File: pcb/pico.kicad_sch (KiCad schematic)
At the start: 13 parts, among them J5 Conn_01x20_Pin, J6 Conn_01x20_Pin, M1 FL, M2 FR, M3 RL, M4 RR, U1 TB9051FTG, U14 IR_Transmitter, U2 TB9051FTG, U3 TB9051FTG, U4 TB9051FTG, U6 SN74LVC8T245NSR

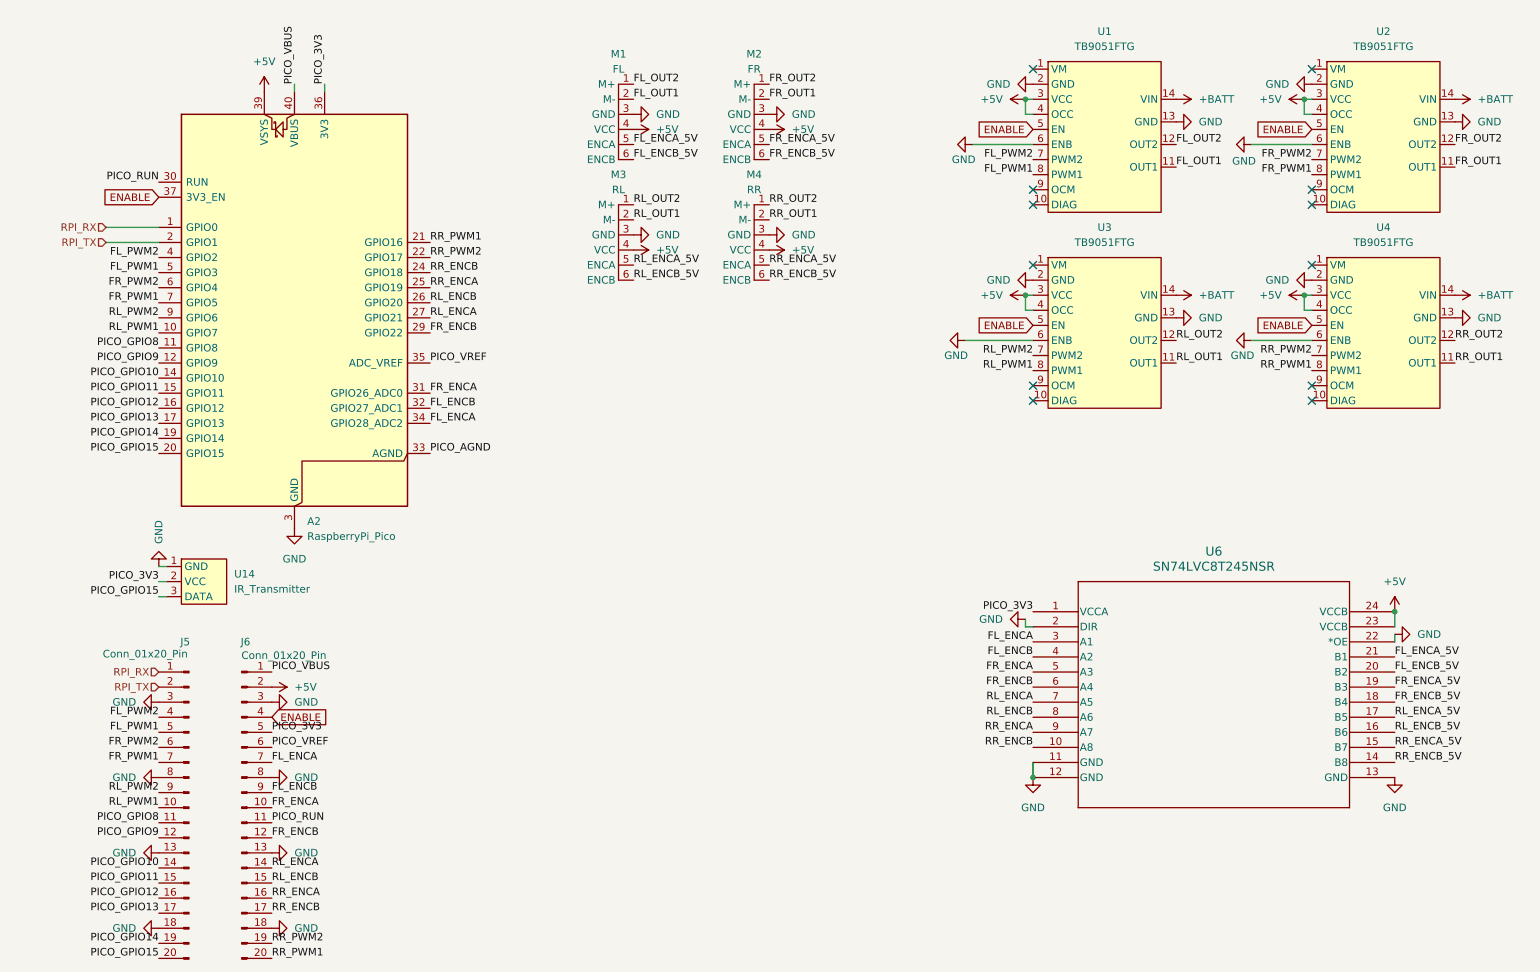
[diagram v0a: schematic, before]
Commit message: Fix ERC issues and layout connectors
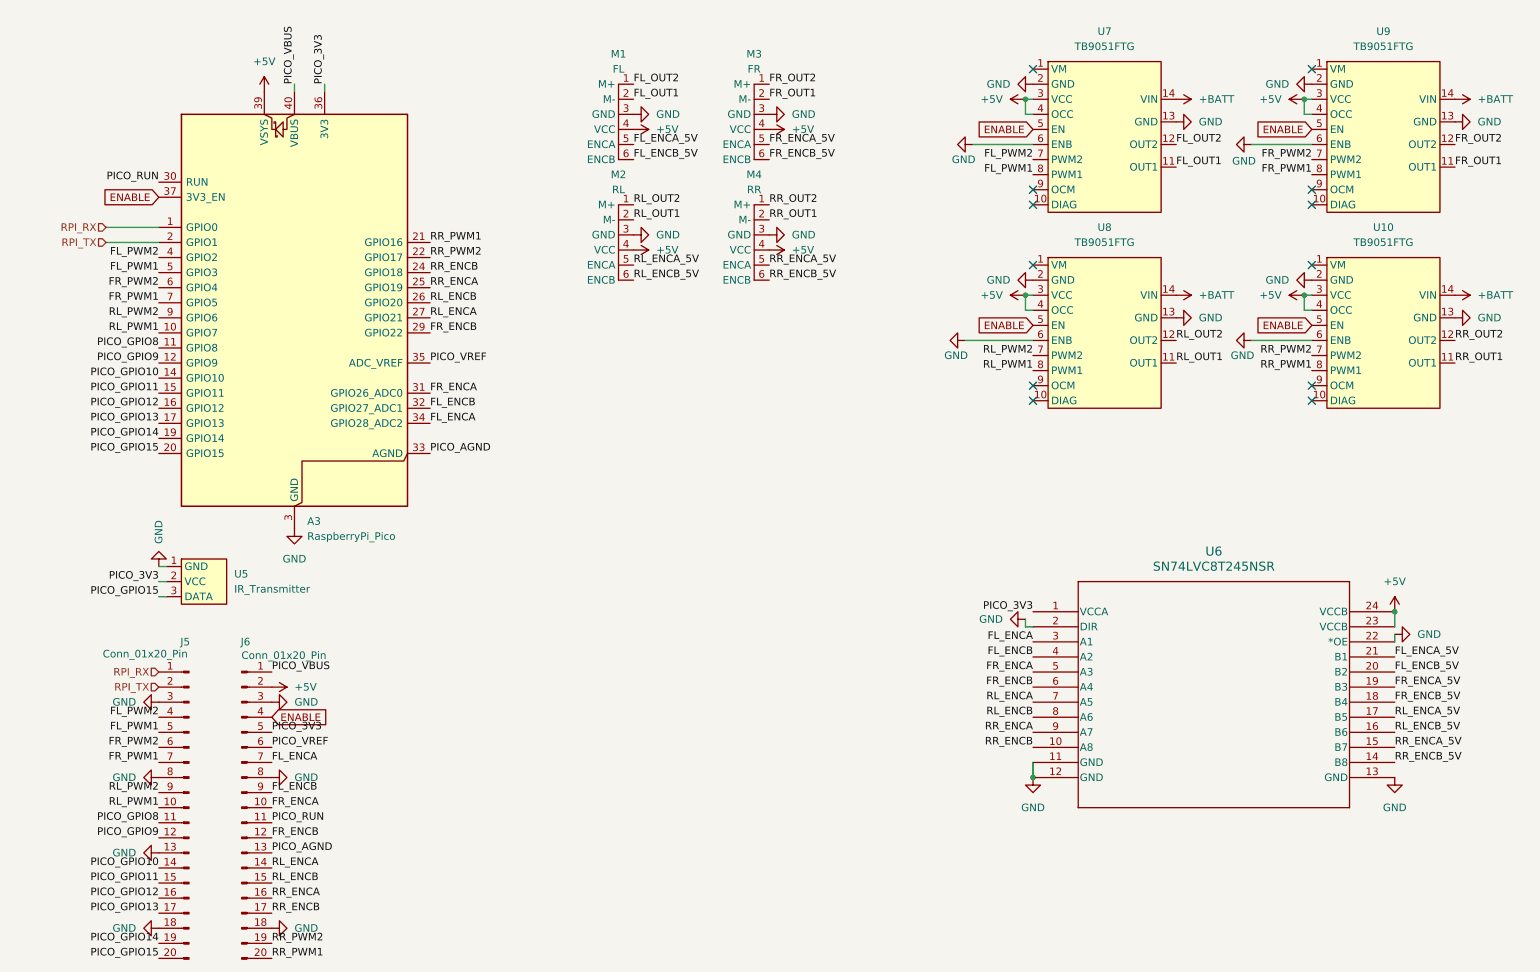
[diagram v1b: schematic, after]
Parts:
- renumbered A2 to A3, M3 to M2, M2 to M3, U4 to U10, U14 to U5, U1 to U7, U3 to U8, U2 to U9
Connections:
- net GND: no longer J6.13 (Pin_13)
- net PICO_AGND: now also J6.13 (Pin_13)

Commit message: Start routing
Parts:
- renumbered A3 to A?, J6 to J?, J5 to J?, M4 to M?, M1 to M?, M2 to M?, M3 to M?, U7 to U?, U9 to U?, U8 to U?, U10 to U?, U6 to U?, U5 to U?
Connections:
- net GND: now also J?.13 (Pin_13); no longer J?.8 (Pin_8)
- net PICO_AGND: now also J?.8 (Pin_8); no longer J?.13 (Pin_13)

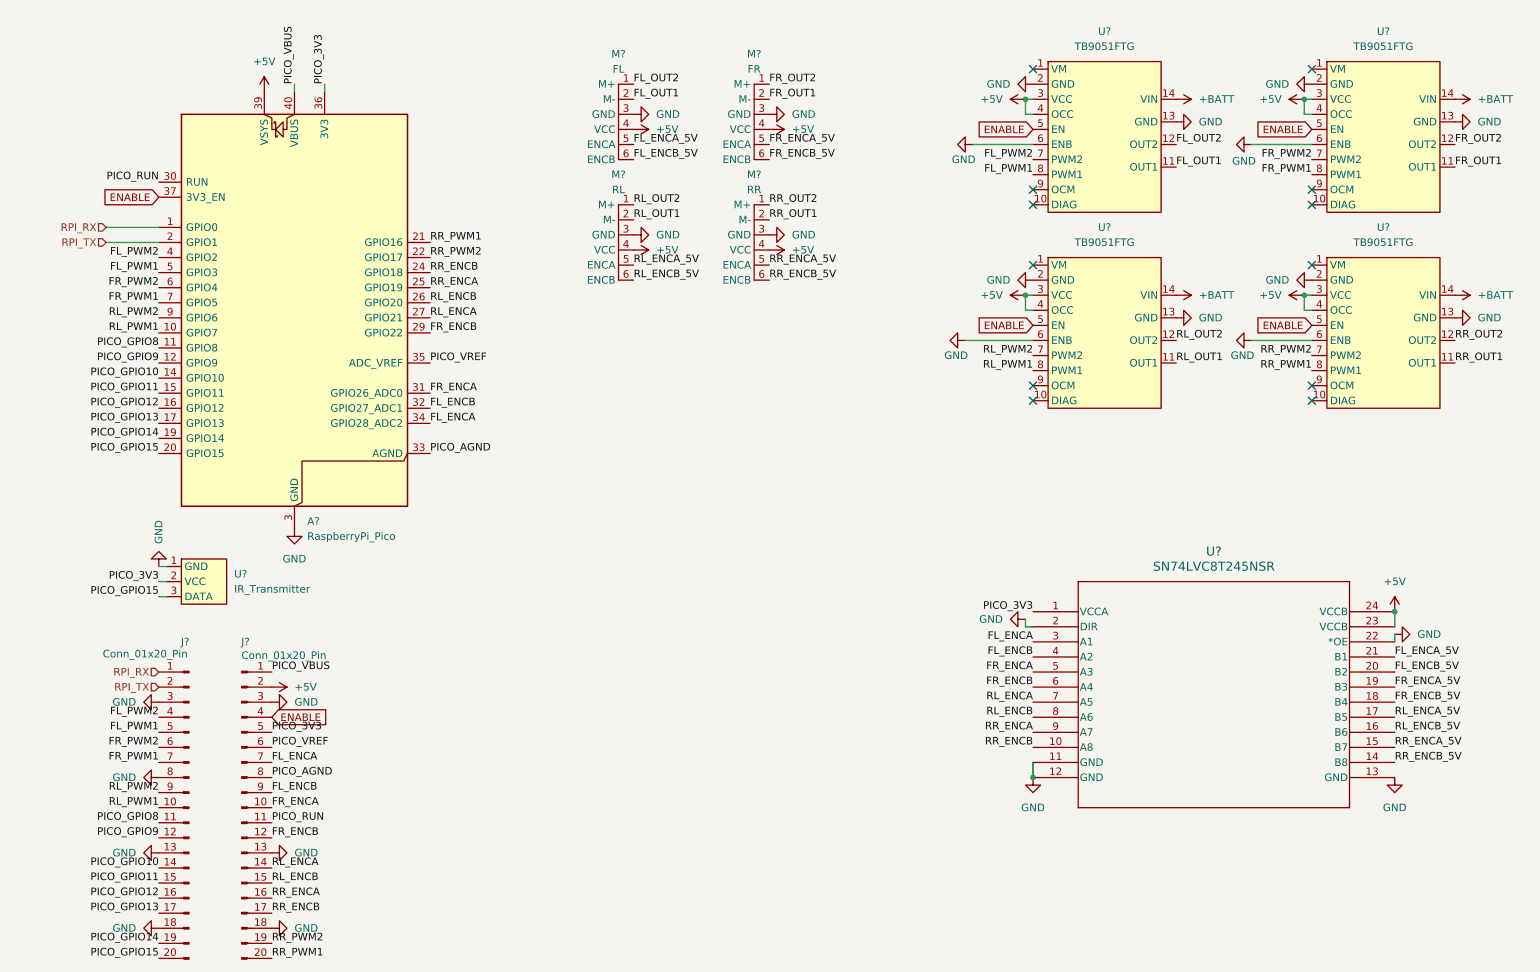
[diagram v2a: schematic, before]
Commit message: Route I2C and planes
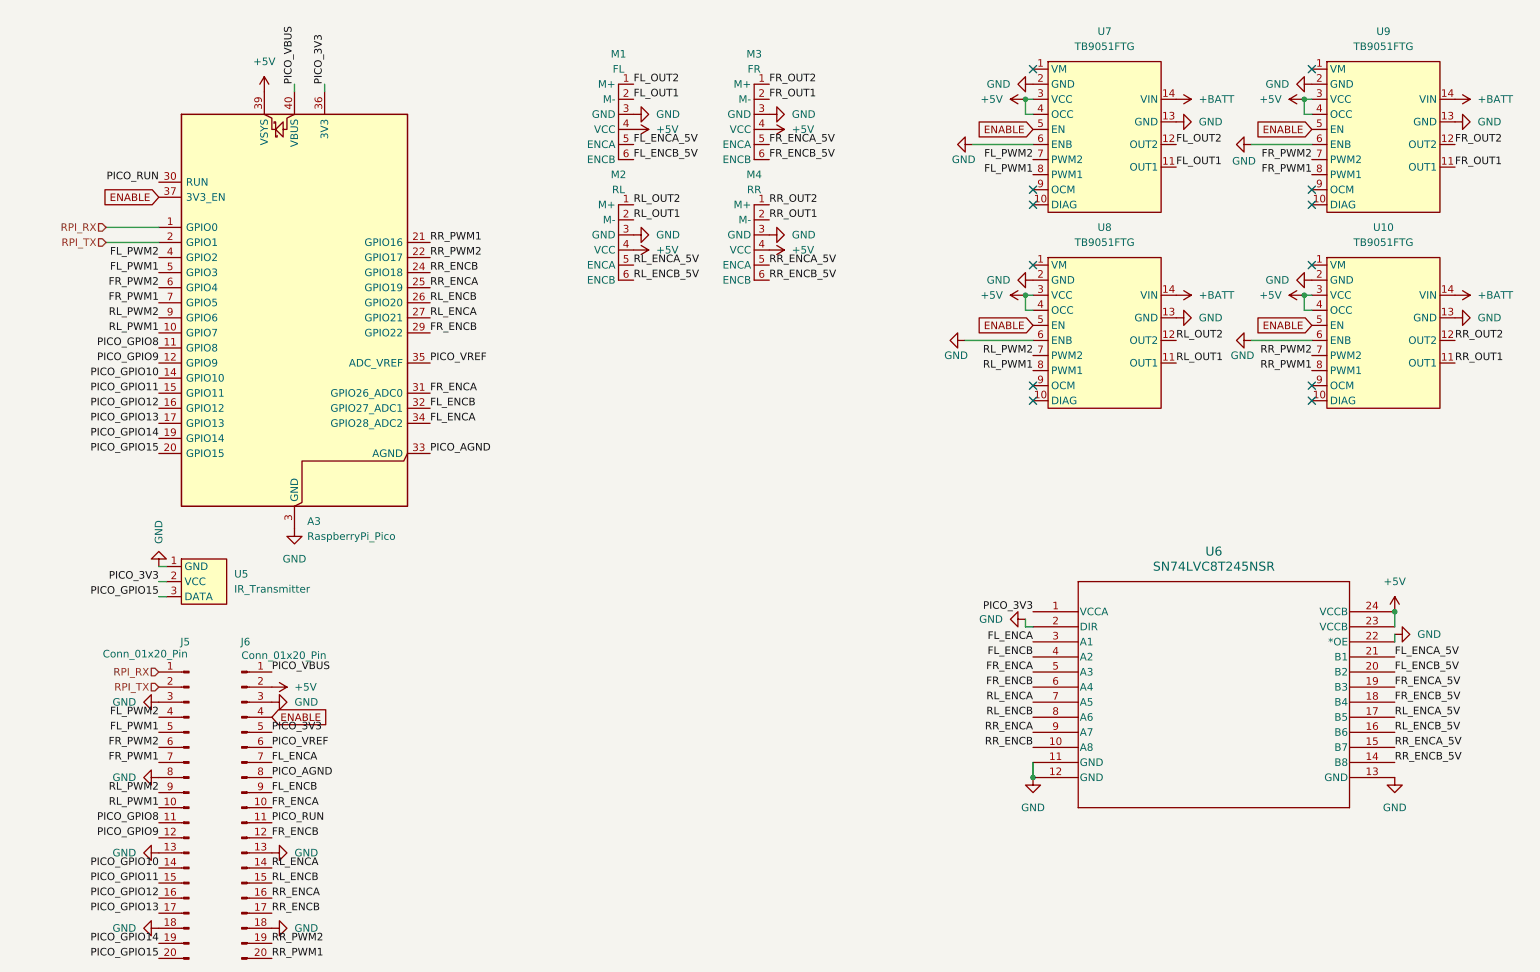
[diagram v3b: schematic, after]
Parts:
- gave numbers to parts that had none: 13
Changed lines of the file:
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@@
 		(dnp no)
 		(fields_autoplaced yes)
-		(property "Reference" "#PWR?"
+		(property "Reference" "#PWR039"
 			(at 129.54 35.56 0)
 			(effects
@@
 		(dnp no)
 		(fields_autoplaced yes)
-		(property "Reference" "#PWR?"
+		(property "Reference" "#PWR030"
 			(at 46.99 157.48 0)
 			(effects
@@
 		(dnp no)
 		(fields_autoplaced yes)
-		(property "Reference" "#PWR?"
+		(property "Reference" "#PWR066"
 			(at 261.62 151.13 0)
 			(effects
@@
 		(dnp no)
 		(fields_autoplaced yes)
-		(property "Reference" "#PWR01"
+		(property "Reference" "#PWR0101"
 			(at 78.74 157.48 0)
 			(effects
@@
 				)
 			)
+			(project "ieee"
+				(path "/de247b43-2c3b-4650-9f65-a404f4d1ae86/a87090f9-d2e3-4dff-b75c-ef59f3dcab82"
+					(reference "#PWR0101")
+					(unit 1)
+				)
+			)
 		)
 	)
@@
 		(dnp no)
 		(fields_autoplaced yes)
-		(property "Reference" "#PWR?"
+		(property "Reference" "#PWR056"
 			(at 220.98 63.5 0)
 			(effects
@@
 		(dnp no)
 		(fields_autoplaced yes)
-		(property "Reference" "#PWR?"
+		(property "Reference" "#PWR048"
 			(at 203.2 30.48 0)
 			(effects
@@
 		(dnp no)
 		(fields_autoplaced yes)
-		(property "Reference" "#PWR?"
+		(property "Reference" "#PWR068"
 			(at 278.13 34.29 0)
 			(effects
@@
 		(dnp no)
 		(fields_autoplaced yes)
-		(property "Reference" "#PWR?"
+		(property "Reference" "#PWR061"
 			(at 250.19 63.5 0)
 			(effects
@@
 		(dnp no)
 		(fields_autoplaced yes)
-		(property "Reference" "#PWR?"
+		(property "Reference" "#PWR052"
 			(at 194.31 60.96 0)
 			(effects
@@
 		(dnp no)
 		(fields_autoplaced yes)
-		(property "Reference" "#PWR?"
+		(property "Reference" "#PWR033"
 			(at 68.58 129.54 0)
 			(effects
@@
 		(dnp no)
 		(fields_autoplaced yes)
-		(property "Reference" "#PWR?"
+		(property "Reference" "#PWR031"
 			(at 46.99 170.18 0)
 			(effects
@@
 		(dnp no)
 		(fields_autoplaced yes)
-		(property "Reference" "#PWR?"
+		(property "Reference" "#PWR040"
 			(at 139.7 53.34 0)
 			(effects
@@
 		(dnp no)
 		(fields_autoplaced yes)
-		(property "Reference" "#PWR?"
+		(property "Reference" "#PWR051"
 			(at 194.31 27.94 0)
 			(effects
@@
 		(on_board yes)
 		(dnp no)
-		(property "Reference" "#PWR?"
+		(property "Reference" "#PWR058"
 			(at 231.14 38.1 0)
 			(effects
@@
 		(dnp no)
 		(fields_autoplaced yes)
-		(property "Reference" "#PWR?"
+		(property "Reference" "#PWR042"
 			(at 162.56 33.02 0)
 			(effects
@@
 		(on_board yes)
 		(dnp no)
-		(property "Reference" "#PWR?"
+		(property "Reference" "#PWR050"
 			(at 193.04 118.11 0)
 			(effects
@@
 		(dnp no)
 		(fields_autoplaced yes)
-		(property "Reference" "#PWR?"
+		(property "Reference" "#PWR055"
 			(at 231.14 34.29 0)
 			(effects
@@
 		(dnp no)
 		(fields_autoplaced yes)
-		(property "Reference" "U?"
+		(property "Reference" "U7"
 			(at 212.725 19.05 0)
 			(effects
@@
 		(dnp no)
 		(fields_autoplaced yes)
-		(property "Reference" "#PWR?"
+		(property "Reference" "#PWR044"
 			(at 162.56 53.34 0)
 			(effects
@@
 		(on_board yes)
 		(dnp no)
-		(property "Reference" "#PWR?"
+		(property "Reference" "#PWR032"
 			(at 71.12 33.02 0)
 			(effects
@@
 		(on_board yes)
 		(dnp no)
-		(property "Reference" "J?"
+		(property "Reference" "J6"
 			(at 67.945 121.92 0)
 			(effects
@@
 		(dnp no)
 		(fields_autoplaced yes)
-		(property "Reference" "U?"
+		(property "Reference" "U9"
 			(at 259.715 19.05 0)
 			(effects
@@
 		(dnp no)
 		(fields_autoplaced yes)
-		(property "Reference" "#PWR?"
+		(property "Reference" "#PWR064"
 			(at 261.62 120.65 0)
 			(effects
@@
 		(dnp no)
 		(fields_autoplaced yes)
-		(property "Reference" "#PWR?"
+		(property "Reference" "#PWR070"
 			(at 278.13 67.31 0)
 			(effects
@@
 		(on_board yes)
 		(dnp no)
-		(property "Reference" "#PWR?"
+		(property "Reference" "#PWR027"
 			(at 53.34 102.87 0)
 			(effects
@@
 		(dnp no)
 		(fields_autoplaced yes)
-		(property "Reference" "#PWR?"
+		(property "Reference" "#PWR028"
 			(at 46.99 132.08 0)
 			(effects
@@
 		(dnp no)
 		(fields_autoplaced yes)
-		(property "Reference" "#PWR?"
+		(property "Reference" "#PWR029"
 			(at 46.99 144.78 0)
 			(effects
@@
 		(dnp no)
 		(fields_autoplaced yes)
-		(property "Reference" "#PWR?"
+		(property "Reference" "#PWR067"
 			(at 267.97 30.48 0)
 			(effects
@@
 		(on_board yes)
 		(dnp no)
-		(property "Reference" "#PWR?"
+		(property "Reference" "#PWR047"
 			(at 184.15 38.1 0)
 			(effects
@@
 		(dnp no)
 		(fields_autoplaced yes)
-		(property "Reference" "U?"
+		(property "Reference" "U8"
 			(at 212.725 52.07 0)
 			(effects
@@
 		(dnp no)
 		(fields_autoplaced yes)
-		(property "Reference" "#PWR?"
+		(property "Reference" "#PWR060"
 			(at 250.19 30.48 0)
 			(effects
@@
 		(on_board yes)
 		(dnp no)
-		(property "Reference" "U?"
+		(property "Reference" "U10"
 			(at 259.715 52.07 0)
 			(effects
@@
 		(dnp no)
 		(fields_autoplaced yes)
-		(property "Reference" "M?"
+		(property "Reference" "M4"
 			(at 153.67 43.18 0)
 			(effects
@@
 		(dnp no)
 		(fields_autoplaced yes)
-		(property "Reference" "#PWR?"
+		(property "Reference" "#PWR049"
 			(at 203.2 63.5 0)
 			(effects
@@
 		(dnp no)
 		(fields_autoplaced yes)
-		(property "Reference" "M?"
+		(property "Reference" "M1"
 			(at 130.81 22.86 0)
 			(effects
@@
 		(dnp no)
 		(fields_autoplaced yes)
-		(property "Reference" "U?"
+		(property "Reference" "U6"
 			(at 231.14 106.68 0)
 			(effects
@@
 		(on_board yes)
 		(dnp no)
-		(property "Reference" "#PWR?"
+		(property "Reference" "#PWR059"
 			(at 231.14 71.12 0)
 			(effects
@@
 		(dnp no)
 		(fields_autoplaced yes)
-		(property "Reference" "#PWR?"
+		(property "Reference" "#PWR036"
 			(at 78.74 170.18 0)
 			(effects
@@
 		(dnp no)
 		(fields_autoplaced yes)
-		(property "Reference" "M?"
+		(property "Reference" "M2"
 			(at 130.81 43.18 0)
 			(effects
@@
 		(dnp no)
 		(fields_autoplaced yes)
-		(property "Reference" "#PWR?"
+		(property "Reference" "#PWR053"
 			(at 200.66 151.13 0)
 			(effects
@@
 		(dnp no)
 		(fields_autoplaced yes)
-		(property "Reference" "#PWR?"
+		(property "Reference" "#PWR045"
 			(at 152.4 55.88 0)
 			(effects
@@
 		(dnp no)
 		(fields_autoplaced yes)
-		(property "Reference" "#PWR?"
+		(property "Reference" "#PWR062"
 			(at 241.3 27.94 0)
 			(effects
@@
 		(dnp no)
 		(fields_autoplaced yes)
-		(property "Reference" "#PWR?"
+		(property "Reference" "#PWR057"
 			(at 231.14 67.31 0)
 			(effects
@@
 		(dnp no)
 		(fields_autoplaced yes)
-		(property "Reference" "#PWR?"
+		(property "Reference" "#PWR054"
 			(at 220.98 30.48 0)
 			(effects
@@
 		(dnp no)
 		(fields_autoplaced yes)
-		(property "Reference" "#PWR?"
+		(property "Reference" "#PWR038"
 			(at 139.7 33.02 0)
 			(effects
@@
 		(dnp no)
 		(fields_autoplaced yes)
-		(property "Reference" "#PWR?"
+		(property "Reference" "#PWR065"
 			(at 267.97 120.65 0)
 			(effects
@@
 		(dnp no)
 		(fields_autoplaced yes)
-		(property "Reference" "#PWR?"
+		(property "Reference" "#PWR041"
 			(at 129.54 55.88 0)
 			(effects
@@
 		(dnp no)
 		(fields_autoplaced yes)
-		(property "Reference" "#PWR?"
+		(property "Reference" "#PWR043"
 			(at 152.4 35.56 0)
 			(effects
@@
 		(dnp no)
 		(fields_autoplaced yes)
-		(property "Reference" "#PWR?"
+		(property "Reference" "#PWR034"
 			(at 78.74 132.08 0)
 			(effects
@@
 		(on_board yes)
 		(dnp no)
-		(property "Reference" "J?"
+		(property "Reference" "J5"
 			(at 57.785 121.92 0)
 			(effects
@@
 		(on_board yes)
 		(dnp no)
-		(property "Reference" "#PWR?"
+		(property "Reference" "#PWR046"
 			(at 182.88 71.12 0)
 			(effects
@@
 		(dnp no)
 		(fields_autoplaced yes)
-		(property "Reference" "U?"
+		(property "Reference" "U5"
 			(at 66.04 110.4899 0)
 			(effects
@@
 		(dnp no)
 		(fields_autoplaced yes)
-		(property "Reference" "M?"
+		(property "Reference" "M3"
 			(at 153.67 22.86 0)
 			(effects
@@
 		(on_board yes)
 		(dnp no)
-		(property "Reference" "A?"
+		(property "Reference" "A3"
 			(at 78.3433 101.6 0)
 			(effects
@@
 		(dnp no)
 		(fields_autoplaced yes)
-		(property "Reference" "#PWR?"
+		(property "Reference" "#PWR069"
 			(at 267.97 63.5 0)
 			(effects
@@
 		(dnp no)
 		(fields_autoplaced yes)
-		(property "Reference" "#PWR?"
+		(property "Reference" "#PWR037"
 			(at 76.2 109.22 0)
 			(effects
@@
 		(dnp no)
 		(fields_autoplaced yes)
-		(property "Reference" "#PWR?"
+		(property "Reference" "#PWR063"
 			(at 241.3 60.96 0)
 			(effects

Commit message: Finish layout
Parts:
- added C1, C2, C3, C4, C5: 0.1uF, Capacitor_SMD:C_0603_1608Metric_Pad1.08x0.95mm_HandSolder, symbol Device:C
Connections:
- net PICO_GPIO8 is gone; now on net FL_PWM1: A3.11 (GPIO8), J5.11 (Pin_11)
- net PICO_GPIO9 is gone; now on net FL_PWM2: A3.12 (GPIO9), J5.12 (Pin_12)
- net +5V: now also C1.2, C2.2, C4.2
- net FL_PWM1: no longer A3.5 (GPIO3), J5.5 (Pin_5)
- net FL_PWM2: no longer A3.4 (GPIO2), J5.4 (Pin_4)
- net FR_ENCA_5V: now also U6.17 (B5); no longer U6.19 (B3)
- net FR_ENCB_5V: now also U6.16 (B6); no longer U6.18 (B4)
- net FR_PWM1: now also A3.6 (GPIO4), J5.6 (Pin_6); no longer A3.7 (GPIO5), J5.7 (Pin_7)
- net FR_PWM2: now also A3.7 (GPIO5), J5.7 (Pin_7); no longer A3.6 (GPIO4), J5.6 (Pin_6)
- net GND: now also C1.1, C2.1, C3.1, C4.1, C5.1
- net PICO_3V3: now also C3.2, C5.2
- net PICO_GPIO10: now also U5.3 (DATA)
- net PICO_GPIO15: no longer U5.3 (DATA)
- net RL_ENCA_5V: now also U6.19 (B3); no longer U6.17 (B5)
- net RL_ENCB_5V: now also U6.18 (B4); no longer U6.16 (B6)
- net RL_PWM1: now also A3.9 (GPIO6), J5.9 (Pin_9); no longer A3.10 (GPIO7), J5.10 (Pin_10)
- net RL_PWM2: now also A3.10 (GPIO7), J5.10 (Pin_10); no longer A3.9 (GPIO6), J5.9 (Pin_9)
- net RR_PWM1: now also A3.4 (GPIO2), J5.4 (Pin_4); no longer A3.21 (GPIO16), J6.20 (Pin_20)
- net RR_PWM2: now also A3.5 (GPIO3), J5.5 (Pin_5); no longer A3.22 (GPIO17), J6.19 (Pin_19)
- new net PICO_GPIO16: A3.21 (GPIO16), J6.20 (Pin_20)
- new net PICO_GPIO17: A3.22 (GPIO17), J6.19 (Pin_19)
